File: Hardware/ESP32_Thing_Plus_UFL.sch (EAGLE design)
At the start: 43 parts, among them Q1 2.5A/30V, Q2 MBT3904DW1T1, U1 MCP73831, U2 ESP-WROOM-32NARROW, U3 AP2112K-3.3V, U4 CP210X

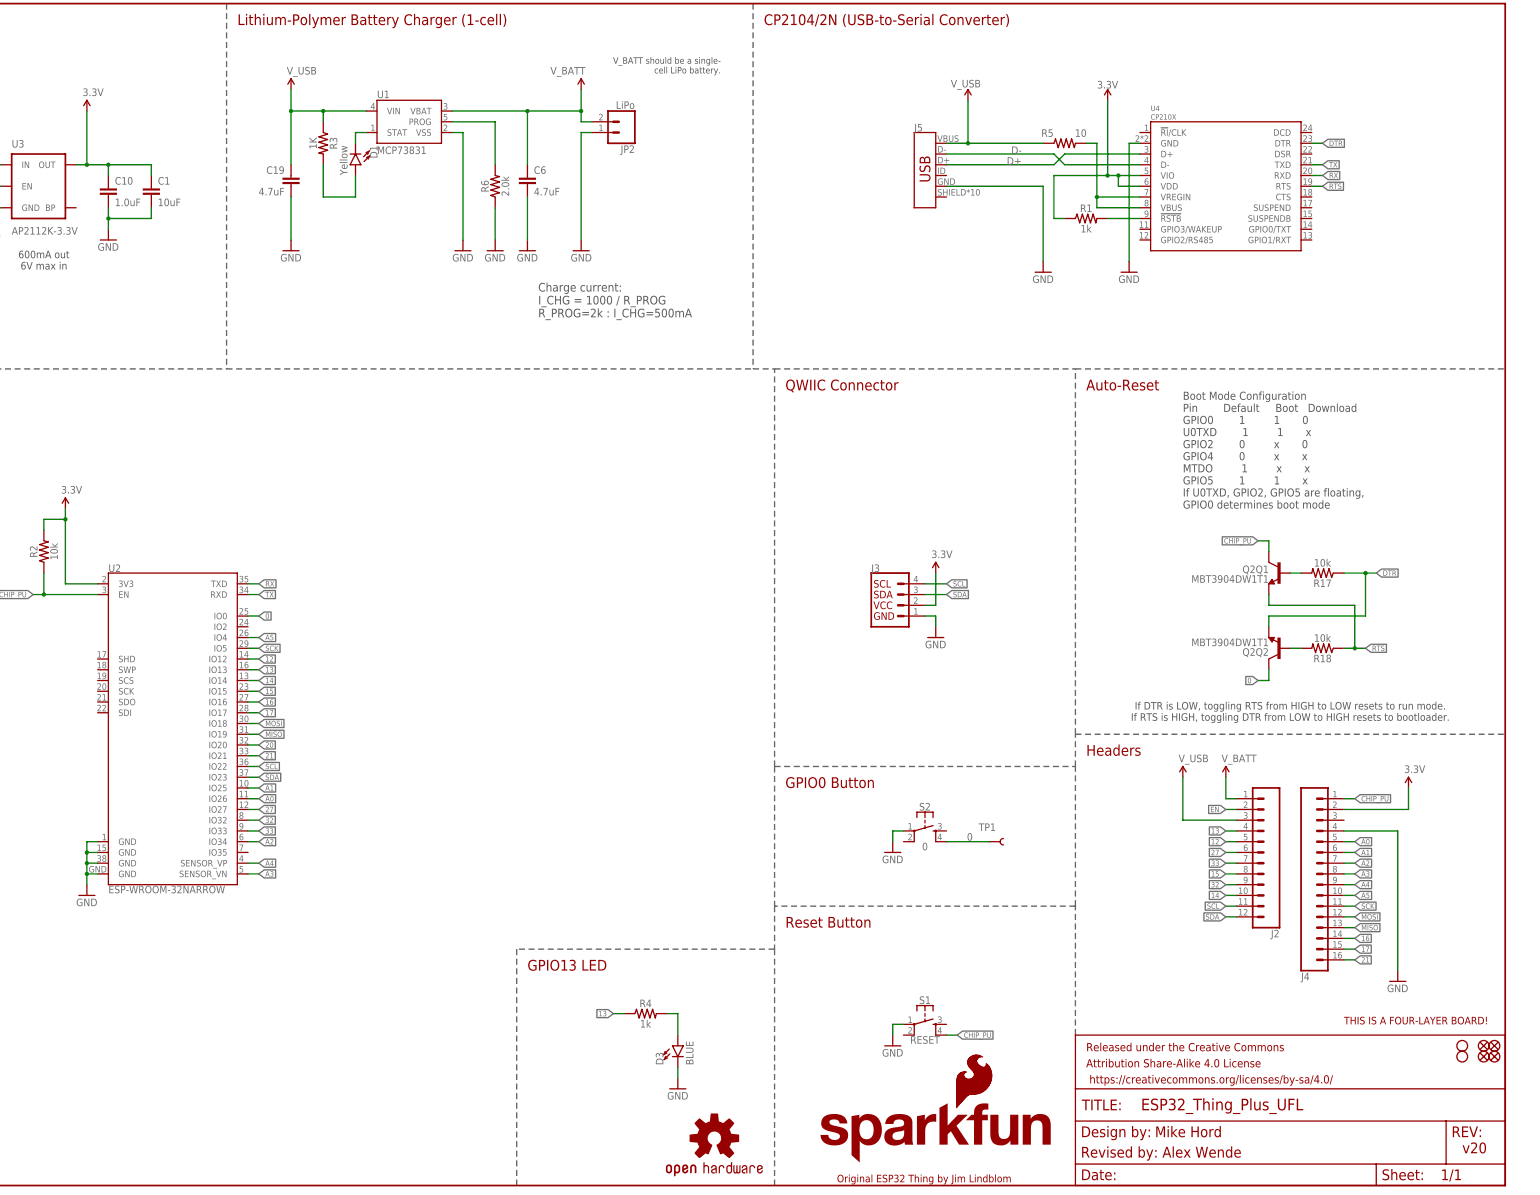
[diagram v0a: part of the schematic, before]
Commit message: switched to u.fl module and modified the CP2104 VBUS input
-u.fl module swapped out
-added standoffs and new measures
-moved product name and logo to top of board
-added in voltage split circuit to vbus input to CP2104
-connected VREGIN pin on CP2104 to 3.3V (previously was connected to vbus)
-changed value of R1 to 2.2K
-added C2 and C3 for additional decoupling caps near CP2104
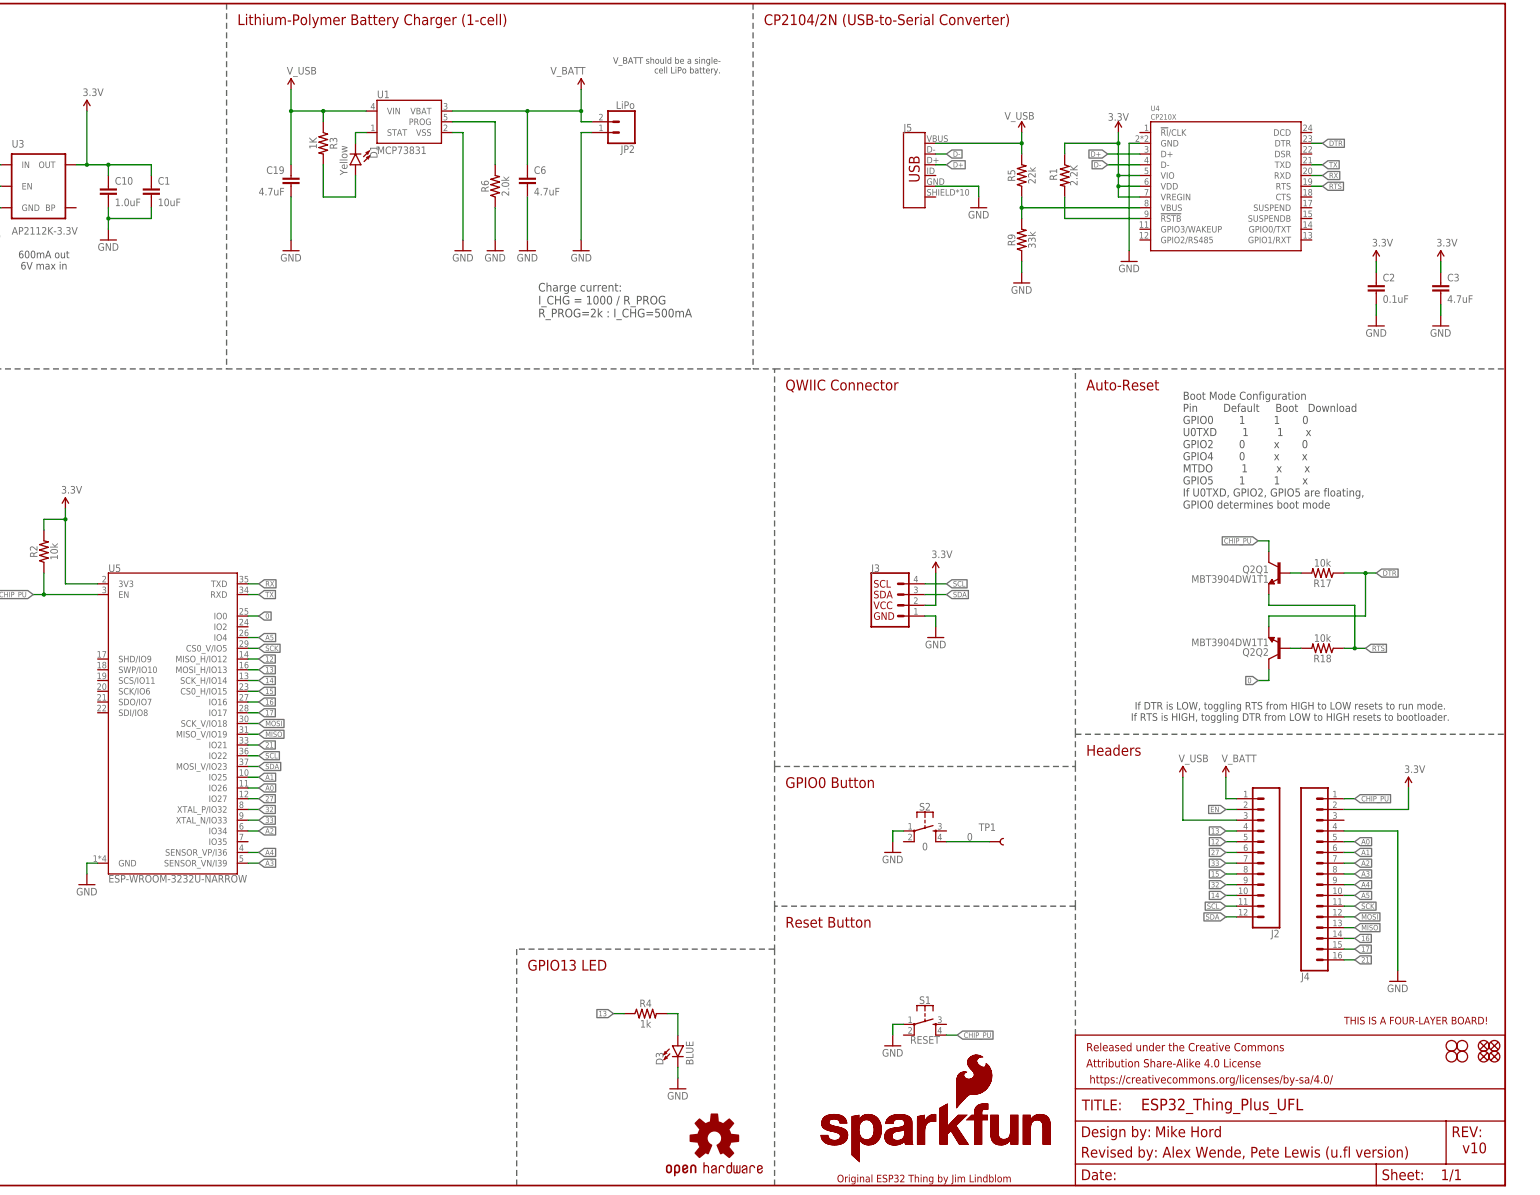
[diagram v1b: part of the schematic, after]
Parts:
- removed U2: ESP-WROOM-32NARROW, SparkFun-RF:ESP-WROOM-32NARROW
- added C2: 0.1uF, SparkFun-Capacitors:0.1UF-0402T-16V-10%
- added C3: 4.7uF, SparkFun-Capacitors:4.7UF-0402_TIGHT-6.3V-20%-X5R
- added H3, H4: STAND-OFFTIGHT, SparkFun-Hardware:STAND-OFFTIGHT
- added LOGO5: SFE_LOGO_NAME_FLAME.1_INCH, SparkFun-Aesthetics:SFE_LOGO_NAME_FLAME.1_INCH
- added R9: 33k, SparkFun-Resistors:33KOHM-0402T-1/16W-1%
- added U5: ESP-WROOM-3232U-NARROW, esp-wroom-32u:ESP-WROOM-3232U-NARROW
- C19, C6: device SparkFun-Capacitors:4.7UF0603 -> SparkFun-Capacitors:4.7UF-0603-6.3V-(10%)
- R1: value 1k -> 2.2K; device SparkFun-Resistors:1KOHM-0603-1/10W-1% -> SparkFun-Resistors:2.2KOHM-0402-1/16W-1%
- R5: value 10 -> 22k; device SparkFun-Resistors:10OHM-0603-1/10W-5% -> SparkFun-Resistors:22KOHM-0402_TIGHT-1/10W-1%
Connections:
- removed net 20: U2.IO20
- removed net N$3: R5.2, U4.VBUS, U4.VREGIN
- new net N$4: R5.1, R9.2, U4.VBUS
- net 0: now also U5.IO0; no longer U2.IO0
- net 12: now also U5.MISO_H/IO12; no longer U2.IO12
- net 13: now also U5.MOSI_H/IO13; no longer U2.IO13
- net 14: now also U5.SCK_H/IO14; no longer U2.IO14
- net 15: now also U5.CS0_H/IO15; no longer U2.IO15
- net 16: now also U5.IO16; no longer U2.IO16
- net 17: now also U5.IO17; no longer U2.IO17
- net 21: now also U5.IO21; no longer U2.IO21
- net 27: now also U5.IO27; no longer U2.IO27
- net 3.3V: now also C2.1, C3.1, U4.VREGIN, U5.3V3; no longer U2.3V3
- net 32: now also U5.XTAL_P/IO32; no longer U2.IO32
- net 33: now also U5.XTAL_N/IO33; no longer U2.IO33
- net A0: now also U5.IO26; no longer U2.IO26
- net A1: now also U5.IO25; no longer U2.IO25
- net A2: now also U5.IO34; no longer U2.IO34
- net A3: now also U5.SENSOR_VN/I39; no longer U2.SENSOR_VN
- net A4: now also U5.SENSOR_VP/I36; no longer U2.SENSOR_VP
- net A5: now also U5.IO4; no longer U2.IO4
- net CHIP_PU: now also U5.EN; no longer U2.EN
- net GND: now also C2.2, C3.2, R9.1, U5.GND; no longer U2.GND, U2.GND@1, U2.GND@15, U2.GND@38
- net MISO: now also U5.MISO_V/IO19; no longer U2.IO19
- net MOSI: now also U5.SCK_V/IO18; no longer U2.IO18
- net RX: now also U5.TXD; no longer U2.TXD
- net SCK: now also U5.CS0_V/IO5; no longer U2.IO5
- net SCL: now also U5.IO22; no longer U2.IO22
- net SDA: now also U5.MOSI_V/IO23; no longer U2.IO23
- net TX: now also U5.RXD; no longer U2.RXD
- net V_USB: now also R5.2; no longer R5.1
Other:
- note added: "Revised by: Alex Wende, Pete Lewis (u.fl version)"
- note added: "v10"
- note removed: "Revised by: Alex Wende"
- note removed: "v20"
- moved on the sheet: J5, R1, R5

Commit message: post design review changes
-changed R1 to a 10K (pullup on RSTB on CP2102)
-nudged U1 (and nearby passives) down to make more space around pin 13 LED.
-changed all 0402 "standard" footprints to use the "tight". re-routed as necessary.
-made all 4.7uF caps the same 0402 part
-made all 1.0uF caps (qty 2) the same 0402 part (X5R)
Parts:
- C10: device SparkFun-Capacitors:1.0UF-0402-16V-10% -> SparkFun-Capacitors:1.0UF-0402T-16V-10%
- C19, C6: device SparkFun-Capacitors:4.7UF-0603-6.3V-(10%) -> SparkFun-Capacitors:4.7UF-0402_TIGHT-6.3V-20%-X5R
- C7: device SparkFun-Capacitors:1.0UF-0603-16V-10%-X7R -> SparkFun-Capacitors:1.0UF-0402T-16V-10%
- R1: value 2.2K -> 10k; device SparkFun-Resistors:2.2KOHM-0402-1/16W-1% -> SparkFun-Resistors:10KOHM-0603-1/10W-1%
- R8: value 100K -> 100k; device SparkFun-Resistors:100KOHM-0402-1/16W-1% -> SparkFun-Resistors:100KOHM-0402T-1/16W-1%
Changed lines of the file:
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@@
 <part name="GND26" library="SparkFun-Aesthetics" deviceset="GND" device=""/>
 <part name="GND15" library="SparkFun-Aesthetics" deviceset="GND" device=""/>
-<part name="C7" library="SparkFun-Capacitors" deviceset="1.0UF" device="-0603-16V-10%-X7R" value="1.0uF"/>
-<part name="C10" library="SparkFun-Capacitors" deviceset="1.0UF" device="-0402-16V-10%" value="1.0uF"/>
+<part name="C7" library="SparkFun-Capacitors" deviceset="1.0UF" device="-0402T-16V-10%" value="1.0uF"/>
+<part name="C10" library="SparkFun-Capacitors" deviceset="1.0UF" device="-0402T-16V-10%" value="1.0uF"/>
 <part name="GND21" library="SparkFun-Aesthetics" deviceset="GND" device=""/>
 <part name="GND14" library="SparkFun-Aesthetics" deviceset="GND" device=""/>
@@
 <part name="GND11" library="SparkFun-Aesthetics" deviceset="GND" device=""/>
 <part name="GND12" library="SparkFun-Aesthetics" deviceset="GND" device=""/>
-<part name="C6" library="SparkFun-Capacitors" deviceset="4.7UF" device="-0603-6.3V-(10%)" value="4.7uF"/>
+<part name="C6" library="SparkFun-Capacitors" deviceset="4.7UF" device="-0402_TIGHT-6.3V-20%-X5R" value="4.7uF"/>
 <part name="D2" library="SparkFun-DiscreteSemi" deviceset="DIODE-SCHOTTKY" device="-BAT20J" value="1A/23V/620mV"/>
 <part name="R7" library="SparkFun-Resistors" deviceset="10KOHM" device="-0603-1/10W-1%" value="10k"/>
@@
 <part name="SUPPLY25" library="SparkFun-Aesthetics" deviceset="V_BATT" device=""/>
 <part name="SUPPLY27" library="SparkFun-Aesthetics" deviceset="V_BATT" device=""/>
-<part name="C19" library="SparkFun-Capacitors" deviceset="4.7UF" device="-0603-6.3V-(10%)" value="4.7uF"/>
+<part name="C19" library="SparkFun-Capacitors" deviceset="4.7UF" device="-0402_TIGHT-6.3V-20%-X5R" value="4.7uF"/>
 <part name="SUPPLY23" library="SparkFun-Aesthetics" deviceset="V_USB" device=""/>
 <part name="GND41" library="SparkFun-Aesthetics" deviceset="GND" device=""/>
@@
 <part name="GND6" library="SparkFun-Aesthetics" deviceset="GND" device=""/>
 <part name="U4" library="SparkFun-IC-Comms" deviceset="CP2102N" device="" value="CP210X"/>
-<part name="R1" library="SparkFun-Resistors" deviceset="2.2KOHM" device="-0402-1/16W-1%" value="2.2K"/>
+<part name="R1" library="SparkFun-Resistors" deviceset="10KOHM" device="-0603-1/10W-1%" value="10k"/>
 <part name="SUPPLY9" library="SparkFun-PowerSymbols" deviceset="3.3V" device=""/>
 <part name="GND7" library="SparkFun-Aesthetics" deviceset="GND" device=""/>
@@
 <part name="R4" library="SparkFun-Resistors" deviceset="1KOHM" device="-0603-1/10W-1%" value="1k"/>
 <part name="GND5" library="SparkFun-Aesthetics" deviceset="GND" device=""/>
-<part name="R8" library="SparkFun-Resistors" deviceset="100KOHM" device="-0402-1/16W-1%" value="100K"/>
+<part name="R8" library="SparkFun-Resistors" deviceset="100KOHM" device="-0402T-1/16W-1%" value="100k"/>
 <part name="LOGO1" library="SparkFun-Aesthetics" deviceset="SFE_LOGO_FLAME" device=".1_INCH"/>
 <part name="LOGO3" library="SparkFun-Aesthetics" deviceset="SFE_LOGO_NAME_FLAME" device=".1_INCH"/>

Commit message: new buzzards, swapped out Miso/Mosi naming
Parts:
- added LOGO6: QWIIC_LOGO_5MM, SparkFun-Aesthetics:QWIIC_LOGO_5MM
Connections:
- net MOSI renamed COPI
- removed net MISO: J4.13, U5.MISO_V/IO19
- new net CIPO: J4.13, U5.CIPO_V/IO19
- net 12: now also U5.CIPO_H/IO12; no longer U5.MISO_H/IO12
- net 13: now also U5.COPI_H/IO13; no longer U5.MOSI_H/IO13
- net SDA: now also U5.COPI_V/IO23; no longer U5.MOSI_V/IO23
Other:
- moved on the sheet: D3, R4, S1
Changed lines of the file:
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@@
 <part name="SUPPLY2" library="SparkFun-PowerSymbols" deviceset="3.3V" device=""/>
 <part name="SUPPLY10" library="SparkFun-PowerSymbols" deviceset="3.3V" device=""/>
+<part name="LOGO6" library="SparkFun-Aesthetics" deviceset="QWIIC_LOGO" device="_5MM" value="QWIIC_LOGO_5MM"/>
 </parts>
 <sheets>
@@
 </plain>
 <instances>
-<instance part="S1" gate="G$1" x="294.64" y="38.1" smashed="yes">
-<attribute name="NAME" x="294.64" y="42.926" size="1.778" layer="95" font="vector" align="bottom-center"/>
-<attribute name="VALUE" x="294.64" y="35.306" size="1.778" layer="96" font="vector" align="top-center"/>
-</instance>
-<instance part="GND1" gate="1" x="287.02" y="33.02" smashed="yes">
-<attribute name="VALUE" x="284.48" y="30.48" size="1.778" layer="96"/>
+<instance part="S1" gate="G$1" x="294.64" y="33.02" smashed="yes">
+<attribute name="NAME" x="294.64" y="37.846" size="1.778" layer="95" font="vector" align="bottom-center"/>
+<attribute name="VALUE" x="294.64" y="30.226" size="1.778" layer="96" font="vector" align="top-center"/>
+</instance>
+<instance part="GND1" gate="1" x="287.02" y="27.94" smashed="yes">
+<attribute name="VALUE" x="284.48" y="25.4" size="1.778" layer="96"/>
 </instance>
 <instance part="FRAME1" gate="G$1" x="0" y="0" smashed="yes"/>
@@
 <attribute name="VALUE" x="375.92" y="129.286" size="1.778" layer="96" font="vector" rot="R180"/>
 </instance>
-<instance part="LOGO2" gate="G$1" x="244.856" y="11.176" smashed="yes"/>
+<instance part="LOGO2" gate="G$1" x="146.304" y="19.304" smashed="yes"/>
 <instance part="J3" gate="G$1" x="287.02" y="137.16" smashed="yes">
 <attribute name="VALUE" x="281.94" y="131.826" size="1.778" layer="96" font="vector" align="top-left"/>
@@
 <attribute name="VALUE" x="113.284" y="231.521" size="1.778" layer="96" font="vector"/>
 </instance>
-<instance part="D3" gate="G$1" x="236.22" y="33.02" smashed="yes">
-<attribute name="NAME" x="232.791" y="28.448" size="1.778" layer="95" font="vector" rot="R90"/>
-<attribute name="VALUE" x="238.125" y="28.448" size="1.778" layer="96" font="vector" rot="R90" align="top-left"/>
-</instance>
-<instance part="R4" gate="G$1" x="228.6" y="40.64" smashed="yes">
-<attribute name="NAME" x="228.6" y="42.164" size="1.778" layer="95" font="vector" align="bottom-center"/>
-<attribute name="VALUE" x="228.6" y="39.116" size="1.778" layer="96" font="vector" align="top-center"/>
-</instance>
-<instance part="GND5" gate="1" x="236.22" y="22.86" smashed="yes">
-<attribute name="VALUE" x="233.68" y="20.32" size="1.778" layer="96"/>
+<instance part="D3" gate="G$1" x="234.188" y="28.194" smashed="yes">
+<attribute name="NAME" x="230.759" y="23.622" size="1.778" layer="95" font="vector" rot="R90"/>
+<attribute name="VALUE" x="236.093" y="23.622" size="1.778" layer="96" font="vector" rot="R90" align="top-left"/>
+</instance>
+<instance part="R4" gate="G$1" x="226.568" y="35.814" smashed="yes">
+<attribute name="NAME" x="226.568" y="37.338" size="1.778" layer="95" font="vector" align="bottom-center"/>
+<attribute name="VALUE" x="226.568" y="34.29" size="1.778" layer="96" font="vector" align="top-center"/>
+</instance>
+<instance part="GND5" gate="1" x="234.188" y="18.034" smashed="yes">
+<attribute name="VALUE" x="231.648" y="15.494" size="1.778" layer="96"/>
 </instance>
 <instance part="R8" gate="G$1" x="63.5" y="236.22" smashed="yes">
@@
 <attribute name="VALUE" x="63.5" y="234.696" size="1.778" layer="96" font="vector" align="top-center"/>
 </instance>
-<instance part="LOGO1" gate="G$1" x="301.752" y="17.78" smashed="yes"/>
-<instance part="LOGO3" gate="G$1" x="269.24" y="5.08" smashed="yes"/>
+<instance part="LOGO1" gate="G$1" x="84.074" y="18.796" smashed="yes"/>
+<instance part="LOGO3" gate="G$1" x="51.562" y="6.096" smashed="yes"/>
 <instance part="LOGO4" gate="G$1" x="393.7" y="38.1" smashed="yes"/>
 <instance part="FD1" gate="G$1" x="429.26" y="33.02" smashed="yes"/>
@@
 <attribute name="VALUE" x="314.96" y="210.82" size="1.778" layer="96"/>
 </instance>
-<instance part="LOGO5" gate="G$1" x="269.24" y="5.08" smashed="yes"/>
+<instance part="LOGO5" gate="G$1" x="51.562" y="6.096" smashed="yes"/>
 <instance part="C2" gate="G$1" x="401.32" y="210.82" smashed="yes">
 <attribute name="NAME" x="402.844" y="213.741" size="1.778" layer="95" font="vector"/>
@@
 <attribute name="VALUE" x="415.544" y="221.996" size="1.778" layer="96" font="vector"/>
 </instance>
+<instance part="LOGO6" gate="G$1" x="122.174" y="13.462" smashed="yes"/>
 </instances>
 <busses>
@@
 </segment>
 <segment>
-<label x="302.26" y="35.56" size="1.27" layer="95" font="vector" xref="yes"/>
+<label x="302.26" y="30.48" size="1.27" layer="95" font="vector" xref="yes"/>
 <pinref part="S1" gate="G$1" pin="4"/>
-<wire x1="299.72" y1="35.56" x2="302.26" y2="35.56" width="0.1524" layer="91"/>
+<wire x1="299.72" y1="30.48" x2="302.26" y2="30.48" width="0.1524" layer="91"/>
 </segment>
 </net>
@@
 <segment>
 <pinref part="S1" gate="G$1" pin="1"/>
-<wire x1="289.56" y1="38.1" x2="287.02" y2="38.1" width="0.1524" layer="91"/>
-<wire x1="287.02" y1="38.1" x2="287.02" y2="35.56" width="0.1524" layer="91"/>
+<wire x1="289.56" y1="33.02" x2="287.02" y2="33.02" width="0.1524" layer="91"/>
+<wire x1="287.02" y1="33.02" x2="287.02" y2="30.48" width="0.1524" layer="91"/>
 <pinref part="GND1" gate="1" pin="GND"/>
 </segment>
@@
 <pinref part="GND5" gate="1" pin="GND"/>
 <pinref part="D3" gate="G$1" pin="C"/>
-<wire x1="236.22" y1="25.4" x2="236.22" y2="27.94" width="0.1524" layer="91"/>
+<wire x1="234.188" y1="20.574" x2="234.188" y2="23.114" width="0.1524" layer="91"/>
 </segment>
 <segment>
@@
 </segment>
 </net>
-<net name="MOSI" class="0">
+<net name="COPI" class="0">
 <segment>
 <pinref part="J4" gate="G$1" pin="12"/>
@@
 </segment>
 </net>
-<net name="MISO" class="0">
+<net name="CIPO" class="0">
 <segment>
 <pinref part="J4" gate="G$1" pin="13"/>
@@
 <wire x1="134.62" y1="106.68" x2="137.16" y2="106.68" width="0.1524" layer="91"/>
 <label x="137.16" y="106.68" size="1.27" layer="95" xref="yes"/>
-<pinref part="U5" gate="G$1" pin="MISO_V/IO19"/>
+<pinref part="U5" gate="G$1" pin="CIPO_V/IO19"/>
 </segment>
 </net>
@@
 <wire x1="134.62" y1="99.06" x2="137.16" y2="99.06" width="0.1524" layer="91"/>
 <label x="137.16" y="99.06" size="1.27" layer="95" xref="yes"/>
-<pinref part="U5" gate="G$1" pin="MOSI_V/IO23"/>
+<pinref part="U5" gate="G$1" pin="COPI_V/IO23"/>
 </segment>
 </net>
@@
 <wire x1="134.62" y1="124.46" x2="137.16" y2="124.46" width="0.1524" layer="91"/>
 <label x="137.16" y="124.46" size="1.27" layer="95" xref="yes"/>
-<pinref part="U5" gate="G$1" pin="MISO_H/IO12"/>
+<pinref part="U5" gate="G$1" pin="CIPO_H/IO12"/>
 </segment>
 </net>
@@
 <segment>
 <pinref part="R4" gate="G$1" pin="1"/>
-<wire x1="223.52" y1="40.64" x2="220.98" y2="40.64" width="0.1524" layer="91"/>
-<label x="220.98" y="40.64" size="1.27" layer="95" rot="R180" xref="yes"/>
+<wire x1="221.488" y1="35.814" x2="218.948" y2="35.814" width="0.1524" layer="91"/>
+<label x="218.948" y="35.814" size="1.27" layer="95" rot="R180" xref="yes"/>
 </segment>
 <segment>
 <wire x1="134.62" y1="121.92" x2="137.16" y2="121.92" width="0.1524" layer="91"/>
 <label x="137.16" y="121.92" size="1.27" layer="95" xref="yes"/>
-<pinref part="U5" gate="G$1" pin="MOSI_H/IO13"/>
+<pinref part="U5" gate="G$1" pin="COPI_H/IO13"/>
 </segment>
 </net>
@@
 <pinref part="D3" gate="G$1" pin="A"/>
 <pinref part="R4" gate="G$1" pin="2"/>
-<wire x1="236.22" y1="35.56" x2="236.22" y2="40.64" width="0.1524" layer="91"/>
-<wire x1="236.22" y1="40.64" x2="233.68" y2="40.64" width="0.1524" layer="91"/>
-</segment>
-</net>
+<wire x1="234.188" y1="30.734" x2="234.188" y2="35.814" width="0.1524" layer="91"/>
+<wire x1="234.188" y1="35.814" x2="231.648" y2="35.814" width="0.1524" layer="91"/>
+</segment>
+</net>
